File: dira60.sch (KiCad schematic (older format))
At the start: 21 parts, among them U0 ATmega32U4-AU, X0 XTAL_GND

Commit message: Routed all cols
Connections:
- net COL2: now also U0.22 (PD5)
- net COL3: now also U0.21 (PD3)
- net COL4: now also U0.20 (PD2)
- net COL5: now also U0.19 (PD1)
- net COL6: now also U0.18 (PD0)
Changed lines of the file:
@@
 Text GLabel 6100 2750 2    50   Input ~ 0
 COL7
-Text GLabel 4625 -75  1    50   Input ~ 0
+Text GLabel 6100 2950 2    50   Input ~ 0
 COL6
-Text GLabel 4025 -75  1    50   Input ~ 0
+Text GLabel 6100 3050 2    50   Input ~ 0
 COL5
-Text GLabel 3450 -75  1    50   Input ~ 0
+Text GLabel 6100 3150 2    50   Input ~ 0
 COL4
-Text GLabel 2850 -50  1    50   Input ~ 0
+Text GLabel 6100 3250 2    50   Input ~ 0
 COL3
-Text GLabel 2100 -100 1    50   Input ~ 0
+Text GLabel 6100 3450 2    50   Input ~ 0
 COL2
 Text GLabel 7150 3700 2    50   Input ~ 0

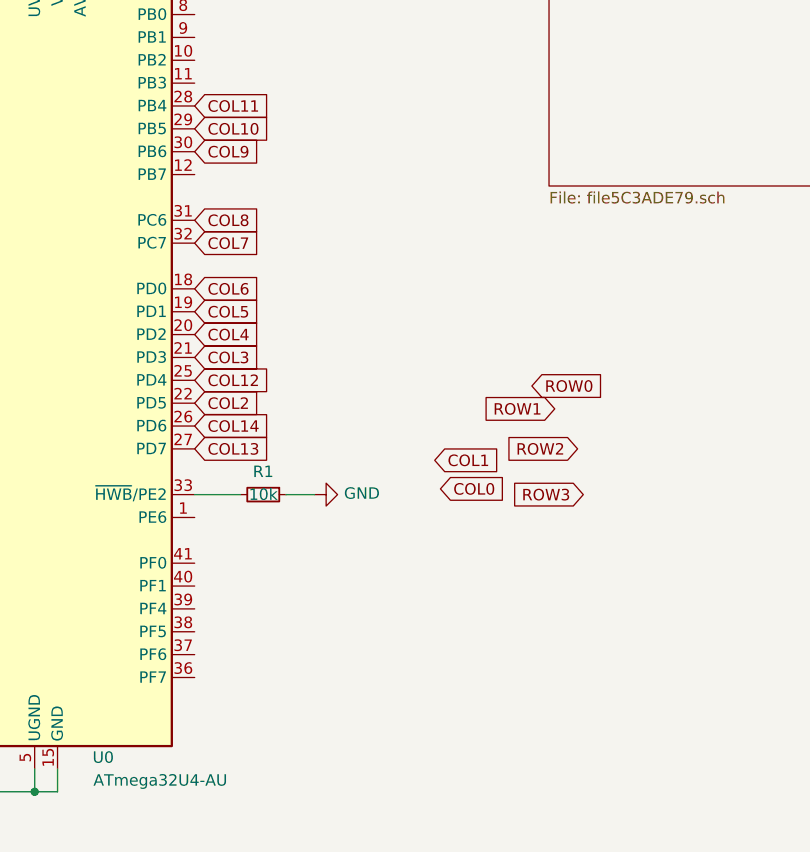
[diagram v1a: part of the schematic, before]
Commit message: Routed rows and cols
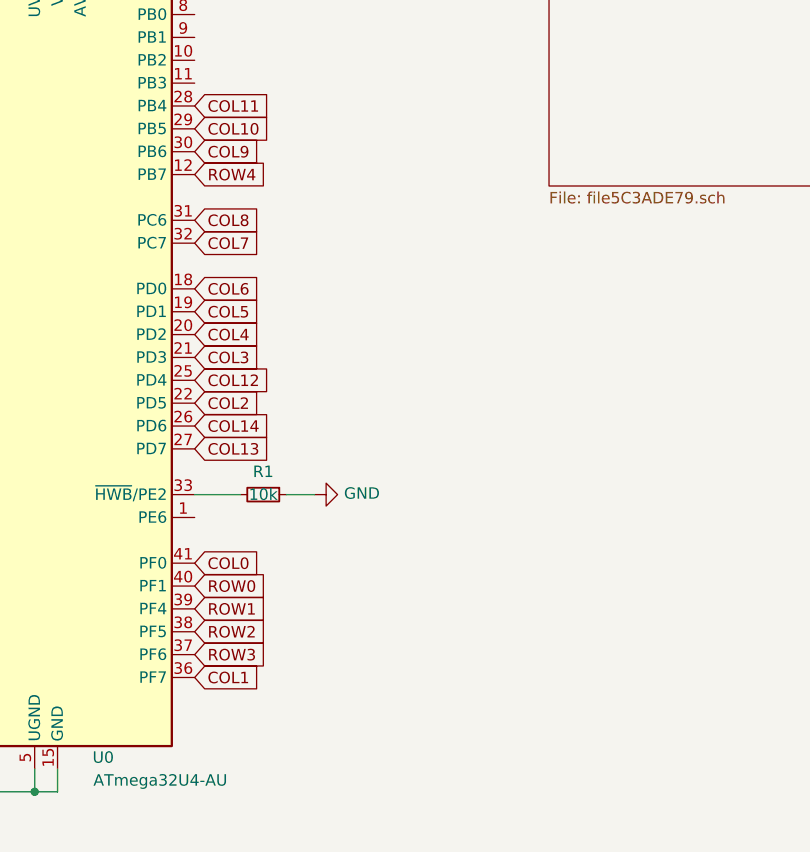
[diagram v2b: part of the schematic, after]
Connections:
- net COL0: now also U0.41 (PF0)
- net COL1: now also U0.36 (PF7)
- net ROW0: now also U0.40 (PF1)
- net ROW1: now also U0.39 (PF4)
- net ROW2: now also U0.38 (PF5)
- net ROW3: now also U0.37 (PF6)
- net ROW4: now reaches U0.12 (PB7)
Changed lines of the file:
@@
 Text GLabel 4900 2150 0    50   Input ~ 0
 XTAL2
-Text GLabel 7575 3375 2    50   Input ~ 0
+Text GLabel 6100 4250 2    50   Input ~ 0
 ROW0
-Text GLabel 7675 3475 0    50   Input ~ 0
+Text GLabel 6100 4350 2    50   Input ~ 0
 ROW1
-Text GLabel 7775 3650 0    50   Input ~ 0
+Text GLabel 6100 4450 2    50   Input ~ 0
 ROW2
-Text GLabel 7800 3850 0    50   Input ~ 0
+Text GLabel 6100 4550 2    50   Input ~ 0
 ROW3
 Text GLabel 6100 3550 2    50   Input ~ 0
@@
 Text GLabel 6100 3450 2    50   Input ~ 0
 COL2
-Text GLabel 7150 3700 2    50   Input ~ 0
+Text GLabel 6100 4650 2    50   Input ~ 0
 COL1
-Text GLabel 7175 3825 2    50   Input ~ 0
+Text GLabel 6100 4150 2    50   Input ~ 0
 COL0
 Text GLabel 6100 3650 2    50   Input ~ 0
@@
 Wire Wire Line
 	9800 5850 10150 5850
+Text GLabel 6100 2450 2    50   Input ~ 0
+ROW4
 $EndSCHEMATC

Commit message: tweaked positions
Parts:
- C0, C1, C10, C11, C2, C3, C4, C5, C6, C7, C8, C9: footprint Capacitor_SMD:C_0805_2012Metric_Pad1.15x1.40mm_HandSolder -> keyboard_parts:C_1608
- R1, R2, R3, R4, R5, R6: footprint Resistor_SMD:R_0805_2012Metric_Pad1.15x1.40mm_HandSolder -> keyboard_parts:R_1608_NOGUIDE
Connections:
- no-connect marks 4 -> 9
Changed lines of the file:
@@
 F 0 "C0" H 3542 4496 50  0000 L CNN
 F 1 "4.7u" H 3542 4405 50  0000 L CNN
-F 2 "Capacitor_SMD:C_0805_2012Metric_Pad1.15x1.40mm_HandSolder" H 3450 4450 50  0001 C CNN
+F 2 "keyboard_parts:C_1608" H 3450 4450 50  0001 C CNN
 F 3 "~" H 3450 4450 50  0001 C CNN
 	1    3450 4450
@@
 F 0 "R2" V 3125 5300 50  0000 C CNN
 F 1 "5.1k" V 3175 5150 50  0000 C CNN
-F 2 "Resistor_SMD:R_0805_2012Metric_Pad1.15x1.40mm_HandSolder" H 3175 5150 50  0001 C CNN
+F 2 "keyboard_parts:R_1608_NOGUIDE" H 3175 5150 50  0001 C CNN
 F 3 "~" H 3175 5150 50  0001 C CNN
 	1    3175 5150
@@
 F 0 "R3" V 3125 5900 50  0000 C CNN
 F 1 "5.1k" V 3175 5750 50  0000 C CNN
-F 2 "Resistor_SMD:R_0805_2012Metric_Pad1.15x1.40mm_HandSolder" H 3175 5750 50  0001 C CNN
+F 2 "keyboard_parts:R_1608_NOGUIDE" H 3175 5750 50  0001 C CNN
 F 3 "~" H 3175 5750 50  0001 C CNN
 	1    3175 5750
@@
 F 0 "C7" V 4550 3050 50  0000 C CNN
 F 1 "1u" V 4750 3050 50  0000 C CNN
-F 2 "Capacitor_SMD:C_0805_2012Metric_Pad1.15x1.40mm_HandSolder" H 4650 3050 50  0001 C CNN
+F 2 "keyboard_parts:C_1608" H 4650 3050 50  0001 C CNN
 F 3 "~" H 4650 3050 50  0001 C CNN
 	1    4650 3050
@@
 F 0 "C1" H 5550 1150 50  0000 L CNN
 F 1 "0.1u" H 5500 1050 50  0000 L CNN
-F 2 "Capacitor_SMD:C_0805_2012Metric_Pad1.15x1.40mm_HandSolder" H 5500 1100 50  0001 C CNN
+F 2 "keyboard_parts:C_1608" H 5500 1100 50  0001 C CNN
 F 3 "~" H 5500 1100 50  0001 C CNN
 	1    5500 1100
@@
 F 0 "C2" V 5850 1250 50  0000 C CNN
 F 1 "0.1u" V 6050 1250 50  0000 C CNN
-F 2 "Capacitor_SMD:C_0805_2012Metric_Pad1.15x1.40mm_HandSolder" H 5950 1250 50  0001 C CNN
+F 2 "keyboard_parts:C_1608" H 5950 1250 50  0001 C CNN
 F 3 "~" H 5950 1250 50  0001 C CNN
 	1    5950 1250
@@
 F 0 "R1" V 6300 3850 50  0000 C CNN
 F 1 "10k" V 6400 3850 50  0000 C CNN
-F 2 "Resistor_SMD:R_0805_2012Metric_Pad1.15x1.40mm_HandSolder" H 6400 3850 50  0001 C CNN
+F 2 "keyboard_parts:R_1608_NOGUIDE" H 6400 3850 50  0001 C CNN
 F 3 "~" H 6400 3850 50  0001 C CNN
 	1    6400 3850
@@
 F 0 "C9" H 9892 5696 50  0000 L CNN
 F 1 "22p" H 9892 5605 50  0000 L CNN
-F 2 "Capacitor_SMD:C_0805_2012Metric_Pad1.15x1.40mm_HandSolder" H 9800 5650 50  0001 C CNN
+F 2 "keyboard_parts:C_1608" H 9800 5650 50  0001 C CNN
 F 3 "~" H 9800 5650 50  0001 C CNN
 	1    9800 5650
@@
 F 0 "C10" H 10592 5696 50  0000 L CNN
 F 1 "22p" H 10592 5605 50  0000 L CNN
-F 2 "Capacitor_SMD:C_0805_2012Metric_Pad1.15x1.40mm_HandSolder" H 10500 5650 50  0001 C CNN
+F 2 "keyboard_parts:C_1608" H 10500 5650 50  0001 C CNN
 F 3 "~" H 10500 5650 50  0001 C CNN
 	1    10500 5650
@@
 F 0 "C3" H 9400 3900 50  0000 L CNN
 F 1 "0.1u" H 9400 3700 50  0000 L CNN
-F 2 "Capacitor_SMD:C_0805_2012Metric_Pad1.15x1.40mm_HandSolder" H 9350 3800 50  0001 C CNN
+F 2 "keyboard_parts:C_1608" H 9350 3800 50  0001 C CNN
 F 3 "~" H 9350 3800 50  0001 C CNN
 	1    9350 3800
@@
 F 0 "C4" H 9750 3900 50  0000 L CNN
 F 1 "0.1u" H 9750 3700 50  0000 L CNN
-F 2 "Capacitor_SMD:C_0805_2012Metric_Pad1.15x1.40mm_HandSolder" H 9700 3800 50  0001 C CNN
+F 2 "keyboard_parts:C_1608" H 9700 3800 50  0001 C CNN
 F 3 "~" H 9700 3800 50  0001 C CNN
 	1    9700 3800
@@
 F 0 "C5" H 10150 3900 50  0000 L CNN
 F 1 "0.1u" H 10150 3700 50  0000 L CNN
-F 2 "Capacitor_SMD:C_0805_2012Metric_Pad1.15x1.40mm_HandSolder" H 10100 3800 50  0001 C CNN
+F 2 "keyboard_parts:C_1608" H 10100 3800 50  0001 C CNN
 F 3 "~" H 10100 3800 50  0001 C CNN
 	1    10100 3800
@@
 F 0 "C6" H 10500 3900 50  0000 L CNN
 F 1 "10u" H 10500 3700 50  0000 L CNN
-F 2 "Capacitor_SMD:C_0805_2012Metric_Pad1.15x1.40mm_HandSolder" H 10450 3800 50  0001 C CNN
+F 2 "keyboard_parts:C_1608" H 10450 3800 50  0001 C CNN
 F 3 "~" H 10450 3800 50  0001 C CNN
 	1    10450 3800
@@
 F 0 "R4" V 2650 6600 50  0000 C CNN
 F 1 "1M" V 2550 6600 50  0000 C CNN
-F 2 "Resistor_SMD:R_0805_2012Metric_Pad1.15x1.40mm_HandSolder" H 2550 6600 50  0001 C CNN
+F 2 "keyboard_parts:R_1608_NOGUIDE" H 2550 6600 50  0001 C CNN
 F 3 "~" H 2550 6600 50  0001 C CNN
 	1    2550 6600
@@
 F 0 "C8" V 2321 6425 50  0000 C CNN
 F 1 "4.7n" V 2412 6425 50  0000 C CNN
-F 2 "Capacitor_SMD:C_0805_2012Metric_Pad1.15x1.40mm_HandSolder" H 2550 6425 50  0001 C CNN
+F 2 "keyboard_parts:C_1608" H 2550 6425 50  0001 C CNN
 F 3 "~" H 2550 6425 50  0001 C CNN
 	1    2550 6425
@@
 F 0 "R5" V 3275 5400 50  0000 C CNN
 F 1 "22" V 3325 5250 50  0000 C CNN
-F 2 "Resistor_SMD:R_0805_2012Metric_Pad1.15x1.40mm_HandSolder" H 3325 5250 50  0001 C CNN
+F 2 "keyboard_parts:R_1608_NOGUIDE" H 3325 5250 50  0001 C CNN
 F 3 "~" H 3325 5250 50  0001 C CNN
 	1    3325 5250
@@
 F 0 "R6" V 3250 5700 50  0000 C CNN
 F 1 "22" V 3300 5550 50  0000 C CNN
-F 2 "Resistor_SMD:R_0805_2012Metric_Pad1.15x1.40mm_HandSolder" H 3300 5550 50  0001 C CNN
+F 2 "keyboard_parts:R_1608_NOGUIDE" H 3300 5550 50  0001 C CNN
 F 3 "~" H 3300 5550 50  0001 C CNN
 	1    3300 5550
@@
 F 0 "C11" H 3617 6246 50  0000 L CNN
 F 1 "4.7u" H 3617 6155 50  0000 L CNN
-F 2 "Capacitor_SMD:C_0805_2012Metric_Pad1.15x1.40mm_HandSolder" H 3525 6200 50  0001 C CNN
+F 2 "keyboard_parts:C_1608" H 3525 6200 50  0001 C CNN
 F 3 "~" H 3525 6200 50  0001 C CNN
 	1    3525 6200
@@
 Text GLabel 6100 2450 2    50   Input ~ 0
 ROW4
+NoConn ~ 6100 3950
+NoConn ~ 6100 1950
+NoConn ~ 6100 1850
+NoConn ~ 6100 1750
+NoConn ~ 6100 2050
 $EndSCHEMATC

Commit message: Routed everything
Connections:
- net COL0: now also U0.40 (PF1); no longer U0.41 (PF0)
- net ROW0: now also U0.12 (PB7); no longer U0.40 (PF1)
- net ROW2: now also U0.41 (PF0); no longer U0.38 (PF5)
- net ROW4: now also U0.38 (PF5); no longer U0.12 (PB7)
- no-connect marks 9 -> 4
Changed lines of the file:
@@
-$EndComp
-$Comp
-L MCU_Microchip_ATmega:ATmega32U4-AU U0
-U 1 1 5C3A488E
-P 5500 3250
-F 0 "U0" H 5700 1500 50  0000 C CNN
-F 1 "ATmega32U4-AU" H 5950 1400 50  0000 C CNN
-F 2 "keyboard_parts:QFN-44-1EP_7x7mm_Pitch0.5mm" H 5500 3250 50  0001 C CIN
-F 3 "http://ww1.microchip.com/downloads/en/DeviceDoc/Atmel-7766-8-bit-AVR-ATmega16U4-32U4_Datasheet.pdf" H 5500 3250 50  0001 C CNN
-	1    5500 3250
-	1    0    0    -1
 $EndComp
 $Comp
@@
 Text GLabel 4900 2150 0    50   Input ~ 0
 XTAL2
-Text GLabel 6100 4250 2    50   Input ~ 0
+Text GLabel 6100 2450 2    50   Input ~ 0
 ROW0
 Text GLabel 6100 4350 2    50   Input ~ 0
 ROW1
-Text GLabel 6100 4450 2    50   Input ~ 0
+Text GLabel 6100 4150 2    50   Input ~ 0
 ROW2
 Text GLabel 6100 4550 2    50   Input ~ 0
@@
 Text GLabel 6100 4650 2    50   Input ~ 0
 COL1
-Text GLabel 6100 4150 2    50   Input ~ 0
+Text GLabel 6100 4250 2    50   Input ~ 0
 COL0
 Text GLabel 6100 3650 2    50   Input ~ 0
 COL13
-Connection ~ 5400 1450
-Connection ~ 5600 1450
-Wire Wire Line
-	5400 1450 5500 1450
-Wire Wire Line
-	5400 1450 4950 1450
 Connection ~ 4500 5150
 Wire Wire Line
@@
 Wire Wire Line
 	9800 5850 10150 5850
-Text GLabel 6100 2450 2    50   Input ~ 0
+Text GLabel 6100 4450 2    50   Input ~ 0
 ROW4
-NoConn ~ 6100 3950
-NoConn ~ 6100 1950
-NoConn ~ 6100 1850
-NoConn ~ 6100 1750
-NoConn ~ 6100 2050
+Connection ~ 5600 1450
+Wire Wire Line
+	5400 1450 4950 1450
+Wire Wire Line
+	5400 1450 5500 1450
+Connection ~ 5400 1450
+$Comp
+L MCU_Microchip_ATmega:ATmega32U4-AU U0
+U 1 1 5C3A488E
+P 5500 3250
+F 0 "U0" H 5700 1500 50  0000 C CNN
+F 1 "ATmega32U4-AU" H 5950 1400 50  0000 C CNN
+F 2 "keyboard_parts:QFN-44-1EP_7x7mm_Pitch0.5mm" H 5500 3250 50  0001 C CIN
+F 3 "http://ww1.microchip.com/downloads/en/DeviceDoc/Atmel-7766-8-bit-AVR-ATmega16U4-32U4_Datasheet.pdf" H 5500 3250 50  0001 C CNN
+	1    5500 3250
+	1    0    0    -1
+$EndComp
 $EndSCHEMATC
